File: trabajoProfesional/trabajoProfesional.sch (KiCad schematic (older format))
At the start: 5 parts, among them U1 1501

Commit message: Add files via upload
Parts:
- SensorPresion1: symbol 2020-08-16_19-32-11:MS583730BA01-50 -> trabajoProfesional-rescue:MS583730BA01-50-2020-08-16_19-32-11
- U1: symbol Trinket:1501 -> trabajoProfesional-rescue:1501-Trinket
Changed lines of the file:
@@
 EESchema Schematic File Version 4
-EELAYER 30 0
+LIBS:trabajoProfesional-cache
+EELAYER 26 0
 EELAYER END
 $Descr A4 11693 8268
@@
 $EndSheet
 $Comp
-L 2020-08-16_19-32-11:MS583730BA01-50 SensorPresion1
+L trabajoProfesional-rescue:MS583730BA01-50-2020-08-16_19-32-11 SensorPresion1
 U 1 1 5F3E65FC
 P 4250 6300
@@
 	5700 1300 2350 1300
 $Comp
-L Trinket:1501 U1
+L trabajoProfesional-rescue:1501-Trinket U1
 U 1 1 5F3DB5D3
 P 4300 2550

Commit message: se agregan los nuevos tamanios de componentes
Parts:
- C6: footprint Capacitor_SMD:C_0201_0603Metric -> Capacitor_SMD:C_0805_2012Metric
- R1, R2: footprint Resistor_SMD:R_0201_0603Metric -> Resistor_SMD:R_0805_2012Metric
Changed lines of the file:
@@
 EESchema Schematic File Version 4
-LIBS:trabajoProfesional-cache
-EELAYER 26 0
+EELAYER 30 0
 EELAYER END
 $Descr A4 11693 8268
@@
 F 0 "C6" V 4748 5700 50  0000 C CNN
 F 1 "100n" V 4839 5700 50  0000 C CNN
-F 2 "Capacitor_SMD:C_0201_0603Metric" H 5038 5550 50  0001 C CNN
+F 2 "Capacitor_SMD:C_0805_2012Metric" H 5038 5550 50  0001 C CNN
 F 3 "~" H 5000 5700 50  0001 C CNN
 	1    5000 5700
@@
 F 0 "R1" H 3470 6246 50  0000 L CNN
 F 1 "10k" H 3470 6155 50  0000 L CNN
-F 2 "Resistor_SMD:R_0201_0603Metric" V 3330 6200 50  0001 C CNN
+F 2 "Resistor_SMD:R_0805_2012Metric" V 3330 6200 50  0001 C CNN
 F 3 "~" H 3400 6200 50  0001 C CNN
 	1    3400 6200
@@
 F 0 "R2" H 3220 6246 50  0000 L CNN
 F 1 "10k" H 3220 6155 50  0000 L CNN
-F 2 "Resistor_SMD:R_0201_0603Metric" V 3080 6200 50  0001 C CNN
+F 2 "Resistor_SMD:R_0805_2012Metric" V 3080 6200 50  0001 C CNN
 F 3 "~" H 3150 6200 50  0001 C CNN
 	1    3150 6200

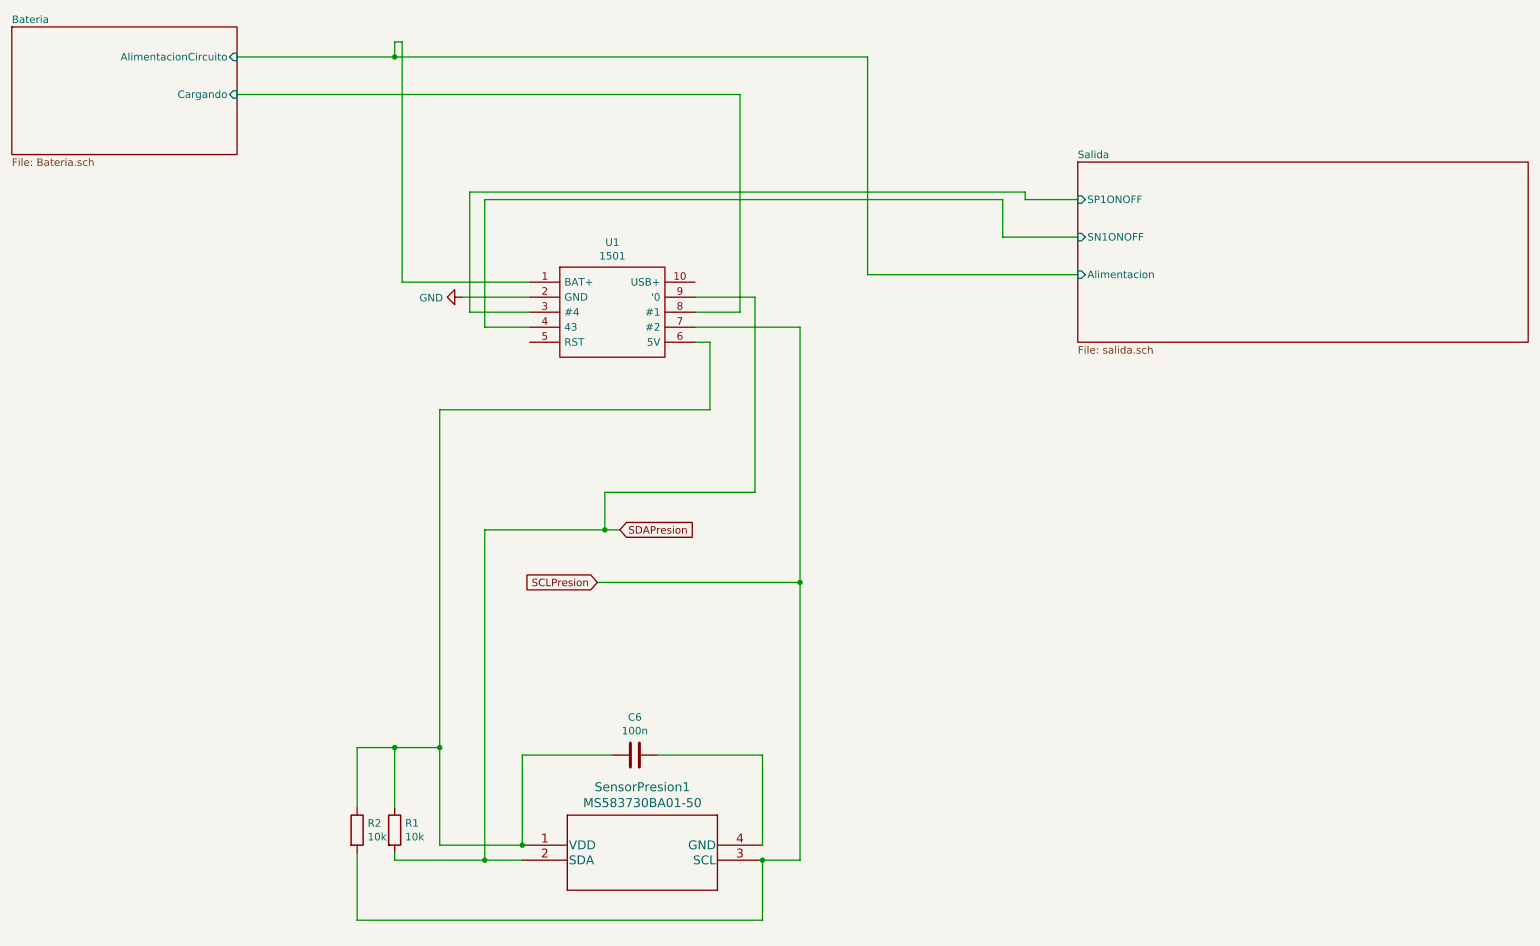
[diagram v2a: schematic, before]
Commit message: Va las nuevas placas modulares, faltan interconexion entre modulos y planos
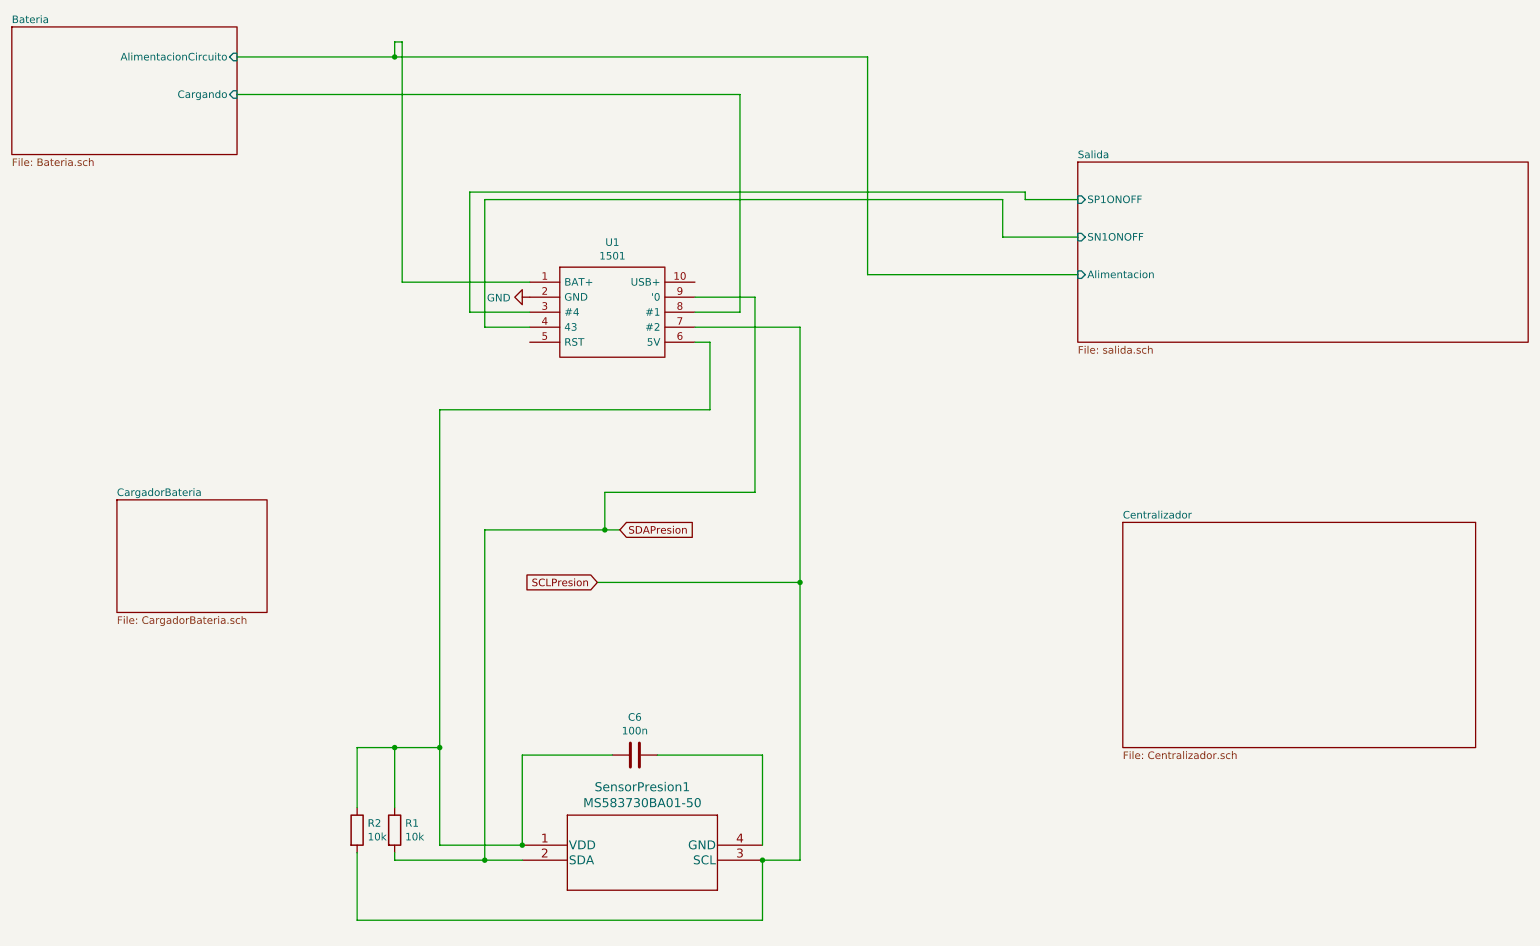
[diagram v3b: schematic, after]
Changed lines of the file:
@@
 $Descr A4 11693 8268
 encoding utf-8
-Sheet 1 3
+Sheet 1 5
 Title ""
 Date ""
@@
 L power:GND #PWR0101
 U 1 1 5F3F217F
-P 3850 2650
-F 0 "#PWR0101" H 3850 2400 50  0001 C CNN
-F 1 "GND" V 3855 2522 50  0000 R CNN
-F 2 "" H 3850 2650 50  0001 C CNN
-F 3 "" H 3850 2650 50  0001 C CNN
-	1    3850 2650
+P 4300 2650
+F 0 "#PWR0101" H 4300 2400 50  0001 C CNN
+F 1 "GND" V 4305 2522 50  0000 R CNN
+F 2 "" H 4300 2650 50  0001 C CNN
+F 3 "" H 4300 2650 50  0001 C CNN
+	1    4300 2650
 	0    1    1    0
 $EndComp
@@
 	5500 2950 5400 2950
 Wire Wire Line
-	3850 2650 4300 2650
-Wire Wire Line
 	3900 2750 4300 2750
 Wire Wire Line
@@
 Wire Wire Line
 	3400 1050 6550 1050
+$Sheet
+S 1550 4000 1000 750
+U 5FFD3686
+F0 "CargadorBateria" 50
+F1 "CargadorBateria.sch" 50
+$EndSheet
+$Sheet
+S 8250 4150 2350 1500
+U 5FFD37EA
+F0 "Centralizador" 50
+F1 "Centralizador.sch" 50
+$EndSheet
 $EndSCHEMATC

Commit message: cuatro placas listas
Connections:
- net GND: now also C6.1, SensorPresion1.4 (GND)
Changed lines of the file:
@@
 $EndComp
 Wire Wire Line
-	5850 6300 5850 5700
-Wire Wire Line
-	5850 5700 5150 5700
+	5850 5700 5600 5700
 Wire Wire Line
 	4250 6300 4250 5700
@@
 F1 "Centralizador.sch" 50
 $EndSheet
+Wire Wire Line
+	5850 6300 5850 5700
+$Comp
+L power:GND #PWR?
+U 1 1 5FFFF8CB
+P 5600 5700
+F 0 "#PWR?" H 5600 5450 50  0001 C CNN
+F 1 "GND" H 5605 5527 50  0000 C CNN
+F 2 "" H 5600 5700 50  0001 C CNN
+F 3 "" H 5600 5700 50  0001 C CNN
+	1    5600 5700
+	1    0    0    -1
+$EndComp
+Connection ~ 5600 5700
+Wire Wire Line
+	5600 5700 5150 5700
 $EndSCHEMATC
